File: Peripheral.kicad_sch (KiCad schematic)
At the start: 2 parts, among them U4 MAX3232ESE+T

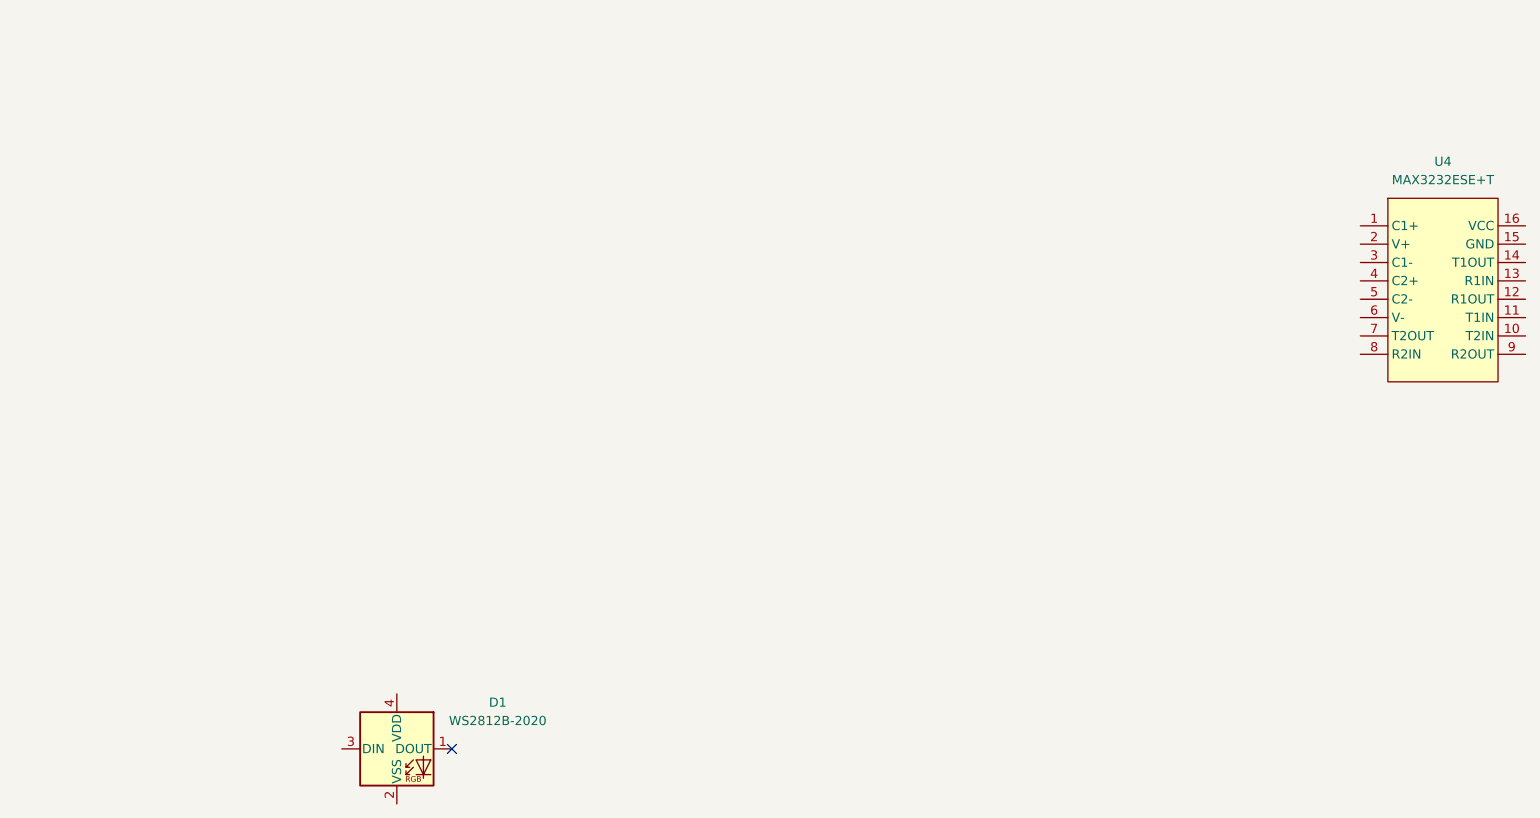
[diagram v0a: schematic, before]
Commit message: [New]: 完成整个原理图绘制和ERC检查
JIRA-ID: N/A

完成整个原理图绘制和ERC检查
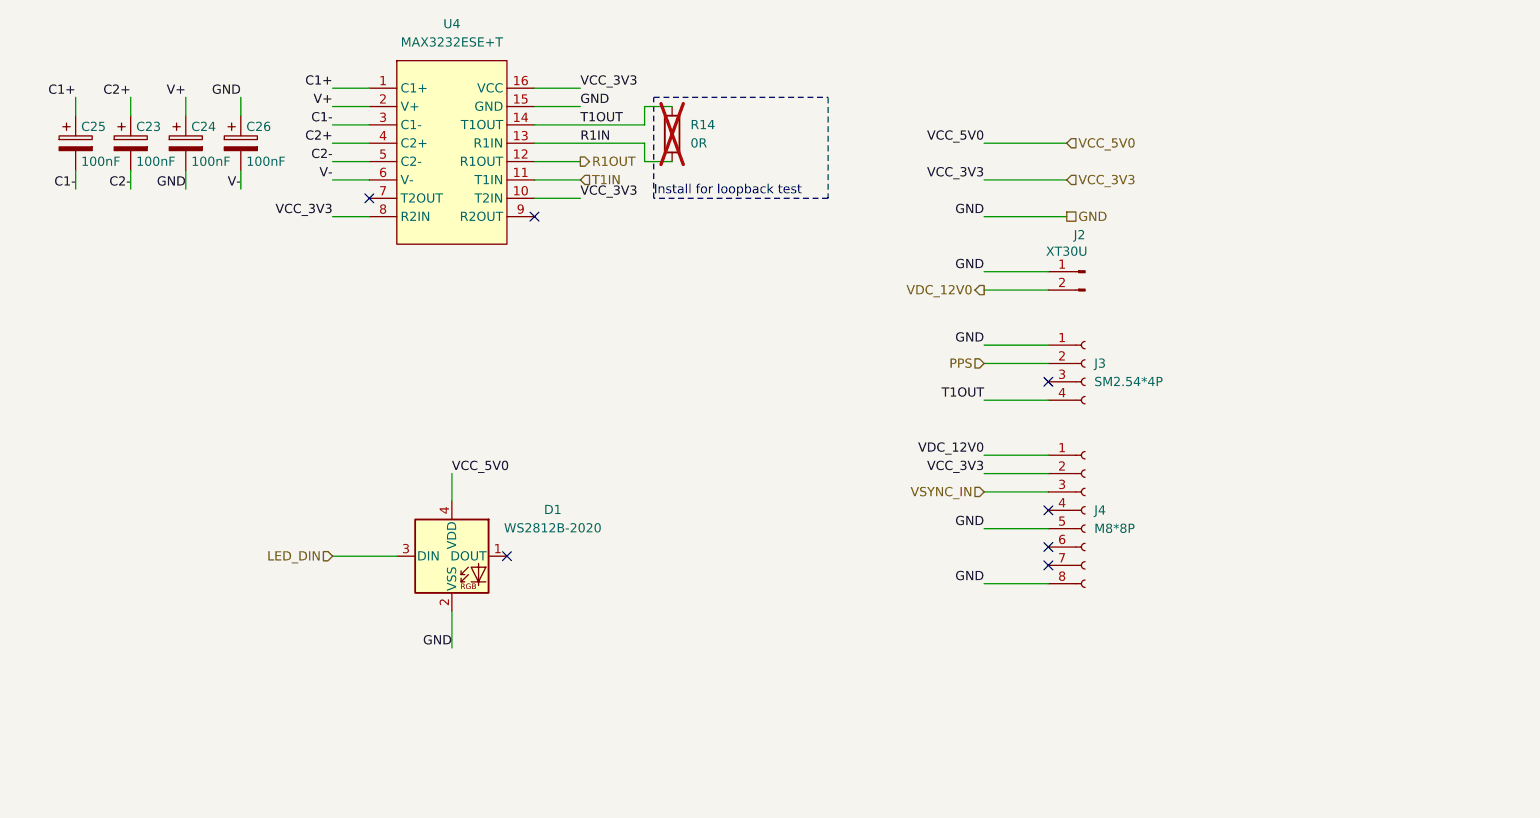
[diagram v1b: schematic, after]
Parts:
- added C23, C24, C25, C26: 100nF, symbol Device:C_Polarized
- added J2: XT30U, symbol Connector:Conn_01x02_Pin
- added J3: SM2.54*4P, symbol Connector:Conn_01x04_Socket
- added J4: M8*8P, symbol Connector:Conn_01x08_Socket
- added R14: 0R, symbol Device:R
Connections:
- net GND: now reaches D1.2 (VSS)
- net GND: now also U4.15 (GND), C24.2, C26.1, J2.1 (Pin_1), J3.1 (Pin_1), J4.5 (Pin_5), J4.8 (Pin_8)
- net LED_DIN: now reaches D1.3 (DIN)
- net VCC_5V0: now reaches D1.4 (VDD)
- net C1+: now reaches U4.1 (C1+)
- net C1+: now also C25.1
- net VCC_3V3: now reaches U4.10 (T2IN)
- net VCC_3V3: now also U4.16 (VCC), U4.8 (R2IN), J4.2 (Pin_2)
- net T1IN: now reaches U4.11 (T1IN)
- net R1OUT: now reaches U4.12 (R1OUT)
- net R1IN: now reaches U4.13 (R1IN)
- net R1IN: now also R14.2
- net T1OUT: now reaches U4.14 (T1OUT)
- net T1OUT: now also J3.4 (Pin_4), R14.1
- net V+: now reaches U4.2 (V+)
- net V+: now also C24.1
- net C1-: now reaches U4.3 (C1-)
- net C1-: now also C25.2
- net C2+: now reaches U4.4 (C2+)
- net C2+: now also C23.1
- net C2-: now reaches U4.5 (C2-)
- net C2-: now also C23.2
- net V-: now reaches U4.6 (V-)
- net V-: now also C26.2
- new net PPS: J3.2 (Pin_2)
- new net VDC_12V0: J2.2 (Pin_2), J4.1 (Pin_1)
- new net VSYNC_IN: J4.3 (Pin_3)
- no-connect marks 1 -> 7
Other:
- note added: "Install for loopback test"
- moved on the sheet: D1, U4

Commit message: [Fix]: 添加雷达供电隔离
JIRA-ID: N/A

添加雷达信号隔离电路，检查原理图错误，新增原理图符号
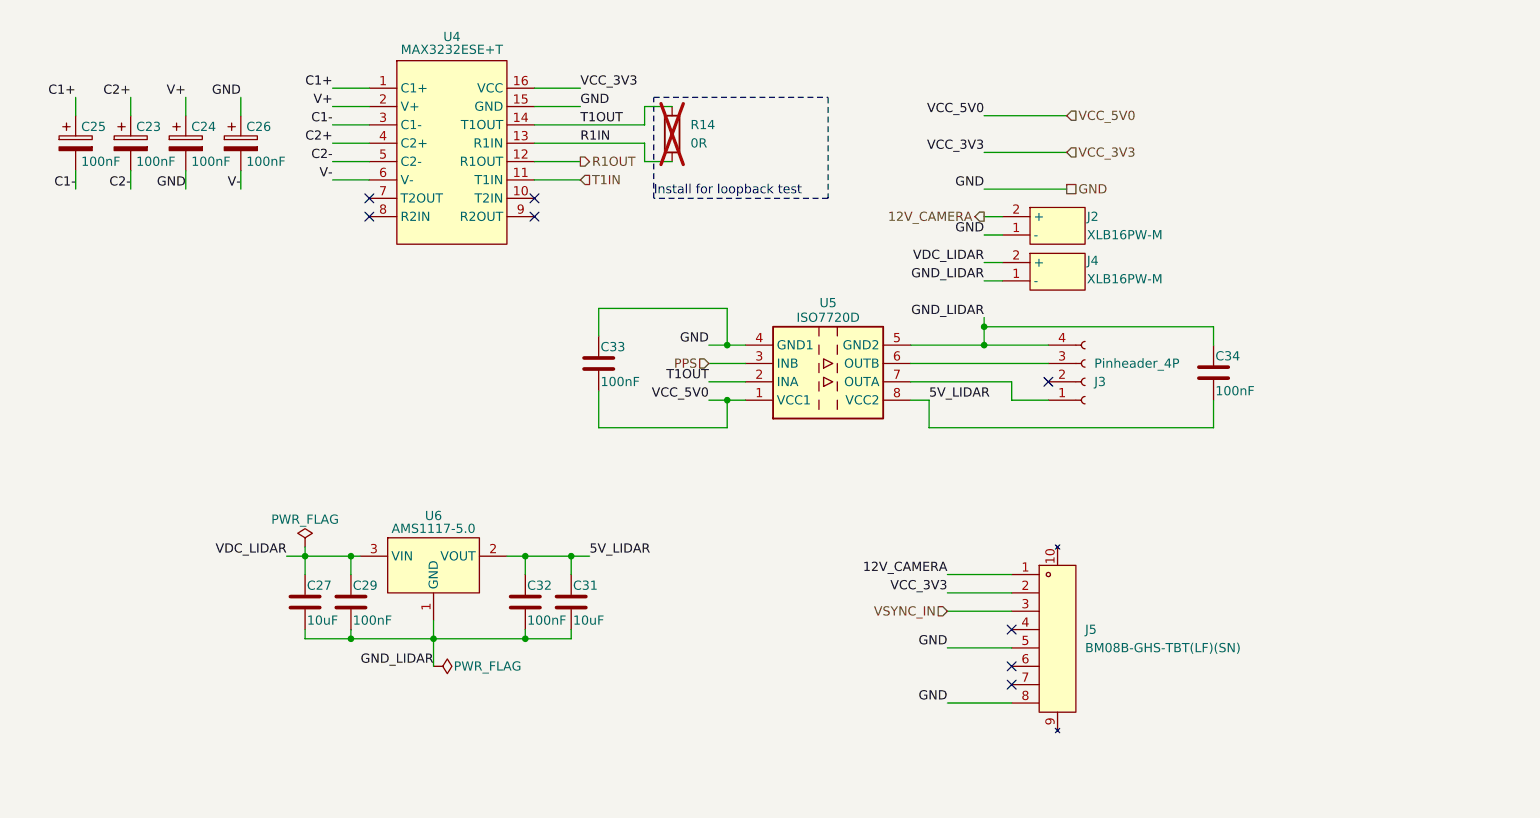
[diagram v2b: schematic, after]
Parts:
- removed D1: WS2812B-2020, LED_SMD:LED_WS2812B-2020_PLCC4_2.0x2.0mm, symbol LED:WS2812B-2020
- removed J2: XT30U, symbol Connector:Conn_01x02_Pin
- removed J4: M8*8P, symbol Connector:Conn_01x08_Socket
- added C27, C31: 10uF, symbol Device:C
- added C29, C32, C33, C34: 100nF, symbol Device:C
- added J2, J4: XLB16PW-M, symbol lidar_camera_sync:XLB16PW-M
- added J5: BM08B-GHS-TBT(LF)(SN), symbol lidar_camera_sync:BM08B-GHS-TBT(LF)(SN)
- added U5: ISO7720D, symbol lidar_camera_sync:ISO7720D
- added U6: AMS1117-5.0, symbol lidar_camera_sync:AMS1117-5.0
- J3: value SM2.54*4P -> Pinheader_4P
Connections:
- net GND: now also C33.1, J2.1 (-), J5.5, J5.8, U5.4 (GND1); no longer J3.1 (Pin_1)
- net PPS: now also U5.3 (INB); no longer J3.2 (Pin_2)
- net T1OUT: now also U5.2 (INA); no longer J3.4 (Pin_4)
- net VCC_3V3: now also J5.2; no longer U4.10 (T2IN), U4.8 (R2IN)
- net VCC_5V0: now also C33.2, U5.1 (VCC1)
- net VSYNC_IN: now also J5.3
- net at J3.3 (Pin_3): now also U5.6 (OUTB)
- new net: J3.1 (Pin_1), U5.7 (OUTA)
- new net 12V_CAMERA: J2.2 (+), J5.1
- new net 5V_LIDAR: C31.1, C32.1, C34.2, U5.8 (VCC2), U6.2 (VOUT), U6.4 (VOUT)
- new net GND_LIDAR: C27.2, C29.2, C31.2, C32.2, C34.1, J3.4 (Pin_4), J4.1 (-), U5.5 (GND2), U6.1 (GND)
- new net VDC_LIDAR: C27.1, C29.1, J4.2 (+), U6.3 (VIN)
- no-connect marks 7 -> 8

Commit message: [Modify]: 完成封装的分配和PCB更新
JIRA-ID: N/A

完成封装的分配和从原理图到PCB的初始更新;完成DRC检查
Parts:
- C25: footprint (none) -> Capacitor_SMD:CP_Elec_4x5.4
- C26: renamed from C23; footprint (none) -> Capacitor_SMD:CP_Elec_4x5.4
- C27: renamed from C24; footprint (none) -> Capacitor_SMD:CP_Elec_4x5.4
- C28: renamed from C26; footprint (none) -> Capacitor_SMD:CP_Elec_4x5.4
- C29: renamed from C27; footprint (none) -> Capacitor_SMD:C_0603_1608Metric
- C30: renamed from C29; footprint (none) -> Capacitor_SMD:C_0603_1608Metric
- C31: renamed from C32; footprint (none) -> Capacitor_SMD:C_0603_1608Metric
- C32: renamed from C31; footprint (none) -> Capacitor_SMD:C_0603_1608Metric
- C33, C34: footprint (none) -> Capacitor_SMD:C_0603_1608Metric
- J2: footprint (none) -> lidar_camera_sync:XLB16PW-M
- J3: renamed from J4; footprint (none) -> lidar_camera_sync:XLB16PW-M
- J4: renamed from J5; footprint (none) -> lidar_camera_sync:BM08B-GHS-TBT(LF)(SN)(N)
- J5: renamed from J3; footprint (none) -> Connector_PinHeader_2.54mm:PinHeader_1x04_P2.54mm_Vertical
- R14: footprint (none) -> Resistor_SMD:R_0603_1608Metric
- U4: renamed from U6; footprint (none) -> lidar_camera_sync:SOT223
- U5: renamed from U4; footprint (none) -> lidar_camera_sync:SOIC16-4.95x8.9_P1.27
- U6: renamed from U5; footprint (none) -> lidar_camera_sync:SOIC8-4.9x5.4_P1.27_NO_EP
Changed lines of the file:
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@@
 		(on_board yes)
 		(dnp no)
-		(property "Reference" "C32"
+		(property "Reference" "C31"
 			(at 94.234 129.794 0)
 			(effects
@@
 			)
 		)
-		(property "Footprint" ""
+		(property "Footprint" "Capacitor_SMD:C_0603_1608Metric"
 			(at 94.9452 135.89 0)
 			(effects
@@
 			(project "lidar_camera_sync"
 				(path "/4d41fa76-12ab-4867-bf30-96d46704f2ab/7a4cebd7-c810-4cc3-a455-f682cc3c6ad0"
-					(reference "C32")
+					(reference "C31")
 					(unit 1)
 				)
@@
 			)
 		)
-		(property "Footprint" ""
+		(property "Footprint" "Capacitor_SMD:C_0603_1608Metric"
 			(at 105.1052 102.87 0)
 			(effects
@@
 		(on_board yes)
 		(dnp no)
-		(property "Reference" "#FLG01"
+		(property "Reference" "#FLG04"
 			(at 63.5 122.555 0)
 			(effects
@@
 			(project ""
 				(path "/4d41fa76-12ab-4867-bf30-96d46704f2ab/7a4cebd7-c810-4cc3-a455-f682cc3c6ad0"
-					(reference "#FLG01")
+					(reference "#FLG04")
 					(unit 1)
 				)
@@
 		(on_board yes)
 		(dnp no)
-		(property "Reference" "C29"
+		(property "Reference" "C30"
 			(at 70.104 129.794 0)
 			(effects
@@
 			)
 		)
-		(property "Footprint" ""
+		(property "Footprint" "Capacitor_SMD:C_0603_1608Metric"
 			(at 70.8152 135.89 0)
 			(effects
@@
 			(project "lidar_camera_sync"
 				(path "/4d41fa76-12ab-4867-bf30-96d46704f2ab/7a4cebd7-c810-4cc3-a455-f682cc3c6ad0"
-					(reference "C29")
+					(reference "C30")
 					(unit 1)
 				)
@@
 		(on_board yes)
 		(dnp no)
-		(property "Reference" "#FLG04"
+		(property "Reference" "#FLG05"
 			(at 83.185 140.97 0)
 			(effects
@@
 			(project "lidar_camera_sync"
 				(path "/4d41fa76-12ab-4867-bf30-96d46704f2ab/7a4cebd7-c810-4cc3-a455-f682cc3c6ad0"
-					(reference "#FLG04")
+					(reference "#FLG05")
 					(unit 1)
 				)
@@
 		(on_board yes)
 		(dnp no)
-		(property "Reference" "U5"
+		(property "Reference" "U6"
 			(at 135.89 90.678 0)
 			(effects
@@
 			)
 		)
-		(property "Footprint" ""
+		(property "Footprint" "lidar_camera_sync:SOIC8-4.9x5.4_P1.27_NO_EP"
 			(at 135.89 100.33 0)
 			(effects
@@
 			(project ""
 				(path "/4d41fa76-12ab-4867-bf30-96d46704f2ab/7a4cebd7-c810-4cc3-a455-f682cc3c6ad0"
-					(reference "U5")
+					(reference "U6")
 					(unit 1)
 				)
@@
 			)
 		)
-		(property "Footprint" ""
+		(property "Footprint" "Resistor_SMD:R_0603_1608Metric"
 			(at 112.522 67.31 90)
 			(effects
@@
 			)
 		)
-		(property "Footprint" ""
+		(property "Footprint" "lidar_camera_sync:XLB16PW-M"
 			(at 167.64 80.01 0)
 			(effects
@@
 		(pin "1"
 		)
+		(pin "3"
+		)
+		(pin "4"
+		)
 		(instances
 			(project ""
@@
 		(on_board yes)
 		(dnp no)
-		(property "Reference" "C31"
+		(property "Reference" "C32"
 			(at 100.584 129.794 0)
 			(effects
@@
 			)
 		)
-		(property "Footprint" ""
+		(property "Footprint" "Capacitor_SMD:C_0603_1608Metric"
 			(at 101.2952 135.89 0)
 			(effects
@@
 			(project "lidar_camera_sync"
 				(path "/4d41fa76-12ab-4867-bf30-96d46704f2ab/7a4cebd7-c810-4cc3-a455-f682cc3c6ad0"
-					(reference "C31")
+					(reference "C32")
 					(unit 1)
 				)
@@
 		(on_board yes)
 		(dnp no)
-		(property "Reference" "J3"
+		(property "Reference" "J5"
 			(at 172.72 101.6001 0)
 			(effects
@@
 			)
 		)
-		(property "Footprint" ""
+		(property "Footprint" "Connector_PinHeader_2.54mm:PinHeader_1x04_P2.54mm_Vertical"
 			(at 171.45 101.6 0)
 			(effects
@@
 			(project "lidar_camera_sync"
 				(path "/4d41fa76-12ab-4867-bf30-96d46704f2ab/7a4cebd7-c810-4cc3-a455-f682cc3c6ad0"
-					(reference "J3")
+					(reference "J5")
 					(unit 1)
 				)
@@
 		(on_board yes)
 		(dnp no)
-		(property "Reference" "J4"
+		(property "Reference" "J3"
 			(at 171.704 84.836 0)
 			(effects
@@
 			)
 		)
-		(property "Footprint" ""
+		(property "Footprint" "lidar_camera_sync:XLB16PW-M"
 			(at 167.64 86.36 0)
 			(effects
@@
 		(pin "1"
 		)
+		(pin "4"
+		)
+		(pin "3"
+		)
 		(instances
 			(project "lidar_camera_sync"
 				(path "/4d41fa76-12ab-4867-bf30-96d46704f2ab/7a4cebd7-c810-4cc3-a455-f682cc3c6ad0"
-					(reference "J4")
+					(reference "J3")
 					(unit 1)
 				)
@@
 		(on_board yes)
 		(dnp no)
-		(property "Reference" "C24"
+		(property "Reference" "C27"
 			(at 47.752 66.294 0)
 			(effects
@@
 			)
 		)
-		(property "Footprint" ""
+		(property "Footprint" "Capacitor_SMD:CP_Elec_4x5.4"
 			(at 47.9552 72.39 0)
 			(effects
@@
 			(project "lidar_camera_sync"
 				(path "/4d41fa76-12ab-4867-bf30-96d46704f2ab/7a4cebd7-c810-4cc3-a455-f682cc3c6ad0"
-					(reference "C24")
+					(reference "C27")
 					(unit 1)
 				)
@@
 		(on_board yes)
 		(dnp no)
-		(property "Reference" "J5"
+		(property "Reference" "J4"
 			(at 171.45 135.8899 0)
 			(effects
@@
 			)
 		)
-		(property "Footprint" ""
+		(property "Footprint" "lidar_camera_sync:BM08B-GHS-TBT(LF)(SN)(N)"
 			(at 167.64 137.16 0)
 			(effects
@@
 			(project ""
 				(path "/4d41fa76-12ab-4867-bf30-96d46704f2ab/7a4cebd7-c810-4cc3-a455-f682cc3c6ad0"
-					(reference "J5")
+					(reference "J4")
 					(unit 1)
 				)
@@
 		(on_board yes)
 		(dnp no)
-		(property "Reference" "C26"
+		(property "Reference" "C28"
 			(at 55.372 66.294 0)
 			(effects
@@
 			)
 		)
-		(property "Footprint" ""
+		(property "Footprint" "Capacitor_SMD:CP_Elec_4x5.4"
 			(at 55.5752 72.39 0)
 			(effects
@@
 			(project "lidar_camera_sync"
 				(path "/4d41fa76-12ab-4867-bf30-96d46704f2ab/7a4cebd7-c810-4cc3-a455-f682cc3c6ad0"
-					(reference "C26")
+					(reference "C28")
 					(unit 1)
 				)
@@
 			)
 		)
-		(property "Footprint" ""
+		(property "Footprint" "Capacitor_SMD:C_0603_1608Metric"
 			(at 190.1952 104.14 0)
 			(effects
@@
 			)
 		)
-		(property "Footprint" ""
+		(property "Footprint" "Capacitor_SMD:CP_Elec_4x5.4"
 			(at 32.7152 72.39 0)
 			(effects
@@
 		(on_board yes)
 		(dnp no)
-		(property "Reference" "U6"
+		(property "Reference" "U4"
 			(at 81.28 120.142 0)
 			(effects
@@
 			)
 		)
-		(property "Footprint" ""
+		(property "Footprint" "lidar_camera_sync:SOT223"
 			(at 81.28 127 0)
 			(effects
@@
 			(project ""
 				(path "/4d41fa76-12ab-4867-bf30-96d46704f2ab/7a4cebd7-c810-4cc3-a455-f682cc3c6ad0"
-					(reference "U6")
+					(reference "U4")
 					(unit 1)
 				)
@@
 		(on_board yes)
 		(dnp no)
-		(property "Reference" "U4"
+		(property "Reference" "U5"
 			(at 83.82 53.848 0)
 			(effects
@@
 			)
 		)
-		(property "Footprint" ""
+		(property "Footprint" "lidar_camera_sync:SOIC16-4.95x8.9_P1.27"
 			(at 83.82 69.85 0)
 			(effects
@@
 			(project ""
 				(path "/4d41fa76-12ab-4867-bf30-96d46704f2ab/7a4cebd7-c810-4cc3-a455-f682cc3c6ad0"
-					(reference "U4")
+					(reference "U5")
 					(unit 1)
 				)
@@
 		(on_board yes)
 		(dnp no)
-		(property "Reference" "C27"
+		(property "Reference" "C29"
 			(at 63.754 129.794 0)
 			(effects
@@
 			)
 		)
-		(property "Footprint" ""
+		(property "Footprint" "Capacitor_SMD:C_0603_1608Metric"
 			(at 64.4652 135.89 0)
 			(effects
@@
 			(project "lidar_camera_sync"
 				(path "/4d41fa76-12ab-4867-bf30-96d46704f2ab/7a4cebd7-c810-4cc3-a455-f682cc3c6ad0"
-					(reference "C27")
+					(reference "C29")
 					(unit 1)
 				)
@@
 		(on_board yes)
 		(dnp no)
-		(property "Reference" "C23"
+		(property "Reference" "C26"
 			(at 40.132 66.294 0)
 			(effects
@@
 			)
 		)
-		(property "Footprint" ""
+		(property "Footprint" "Capacitor_SMD:CP_Elec_4x5.4"
 			(at 40.3352 72.39 0)
 			(effects
@@
 			(project "lidar_camera_sync"
 				(path "/4d41fa76-12ab-4867-bf30-96d46704f2ab/7a4cebd7-c810-4cc3-a455-f682cc3c6ad0"
-					(reference "C23")
-					(unit 1)
-				)
+					(reference "C26")
+					(unit 1)
+				)

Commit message: [Modify]: 添加输入输出去耦电容以及WS2812B灯珠
JIRA-ID: N/A

添加输入输出去耦电容以及WS2812B灯珠
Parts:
- added C24, C35, C36: 22uF, Capacitor_SMD:CP_Elec_6.3x5.4, symbol Device:C_Polarized
- added C37: 100nF, Capacitor_SMD:C_0603_1608Metric, symbol Device:C
- added D3: WS2812B, LED_SMD:LED_WS2812B_PLCC4_5.0x5.0mm_P3.2mm, symbol LED:WS2812B
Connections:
- net 12V_CAMERA: now also C24.1, C36.1
- net GND: now also C24.2, C36.2, C37.2, D3.3 (VSS)
- net GND_LIDAR: now also C35.2
- net VCC_5V0: now also C37.1, D3.1 (VDD)
- net VDC_LIDAR: now also C35.1
- new net LED_DIN: D3.4 (DIN)
- no-connect marks 8 -> 9

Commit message: [Modify]: 修复一些封装错误, 完成基本Layout器件摆放
JIRA-ID: N/A

修复一些封装错误, 完成基本Layout器件摆放
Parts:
- renumbered C25 to C24, C26 to C25, C27 to C26, C37 to C27, C24 to C34, C34 to C37, D3 to STATE1
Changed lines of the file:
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@@
 		(on_board yes)
 		(dnp no)
-		(property "Reference" "C24"
+		(property "Reference" "C34"
 			(at 122.682 133.604 0)
 			(effects
@@
 			(project "lidar_camera_sync"
 				(path "/4d41fa76-12ab-4867-bf30-96d46704f2ab/7a4cebd7-c810-4cc3-a455-f682cc3c6ad0"
-					(reference "C24")
+					(reference "C34")
 					(unit 1)
 				)
@@
 		(on_board yes)
 		(dnp no)
-		(property "Reference" "C37"
+		(property "Reference" "C27"
 			(at 51.816 88.9 90)
 			(effects
@@
 			(project "lidar_camera_sync"
 				(path "/4d41fa76-12ab-4867-bf30-96d46704f2ab/7a4cebd7-c810-4cc3-a455-f682cc3c6ad0"
-					(reference "C37")
+					(reference "C27")
 					(unit 1)
 				)
@@
 		(dnp no)
 		(fields_autoplaced yes)
-		(property "Reference" "D3"
+		(property "Reference" "STATE1"
 			(at 58.42 95.1798 0)
 			(effects
@@
 			(project ""
 				(path "/4d41fa76-12ab-4867-bf30-96d46704f2ab/7a4cebd7-c810-4cc3-a455-f682cc3c6ad0"
-					(reference "D3")
+					(reference "STATE1")
 					(unit 1)
 				)
@@
 		(on_board yes)
 		(dnp no)
-		(property "Reference" "C27"
+		(property "Reference" "C26"
 			(at 47.752 66.294 0)
 			(effects
@@
 			(project "lidar_camera_sync"
 				(path "/4d41fa76-12ab-4867-bf30-96d46704f2ab/7a4cebd7-c810-4cc3-a455-f682cc3c6ad0"
-					(reference "C27")
+					(reference "C26")
 					(unit 1)
 				)
@@
 		(on_board yes)
 		(dnp no)
-		(property "Reference" "C34"
+		(property "Reference" "C37"
 			(at 189.484 98.044 0)
 			(effects
@@
 			(project "lidar_camera_sync"
 				(path "/4d41fa76-12ab-4867-bf30-96d46704f2ab/7a4cebd7-c810-4cc3-a455-f682cc3c6ad0"
-					(reference "C34")
+					(reference "C37")
 					(unit 1)
 				)
@@
 		(on_board yes)
 		(dnp no)
-		(property "Reference" "C25"
+		(property "Reference" "C24"
 			(at 32.512 66.294 0)
 			(effects
@@
 			(project "lidar_camera_sync"
 				(path "/4d41fa76-12ab-4867-bf30-96d46704f2ab/7a4cebd7-c810-4cc3-a455-f682cc3c6ad0"
-					(reference "C25")
+					(reference "C24")
 					(unit 1)
 				)
@@
 		(on_board yes)
 		(dnp no)
-		(property "Reference" "C26"
+		(property "Reference" "C25"
 			(at 40.132 66.294 0)
 			(effects
@@
 			(project "lidar_camera_sync"
 				(path "/4d41fa76-12ab-4867-bf30-96d46704f2ab/7a4cebd7-c810-4cc3-a455-f682cc3c6ad0"
-					(reference "C26")
-					(unit 1)
-				)
+					(reference "C25")
+					(unit 1)
+				)
